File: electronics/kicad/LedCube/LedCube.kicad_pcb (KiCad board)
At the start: 2 copper layers, 20 parts, among them J1 Conn_01x03, J2 Conn_01x03, J3 Conn_01x03, J4 Conn_01x04, J5 COM, J6 Conn_01x02, J7 JTAG, U1 ESP32

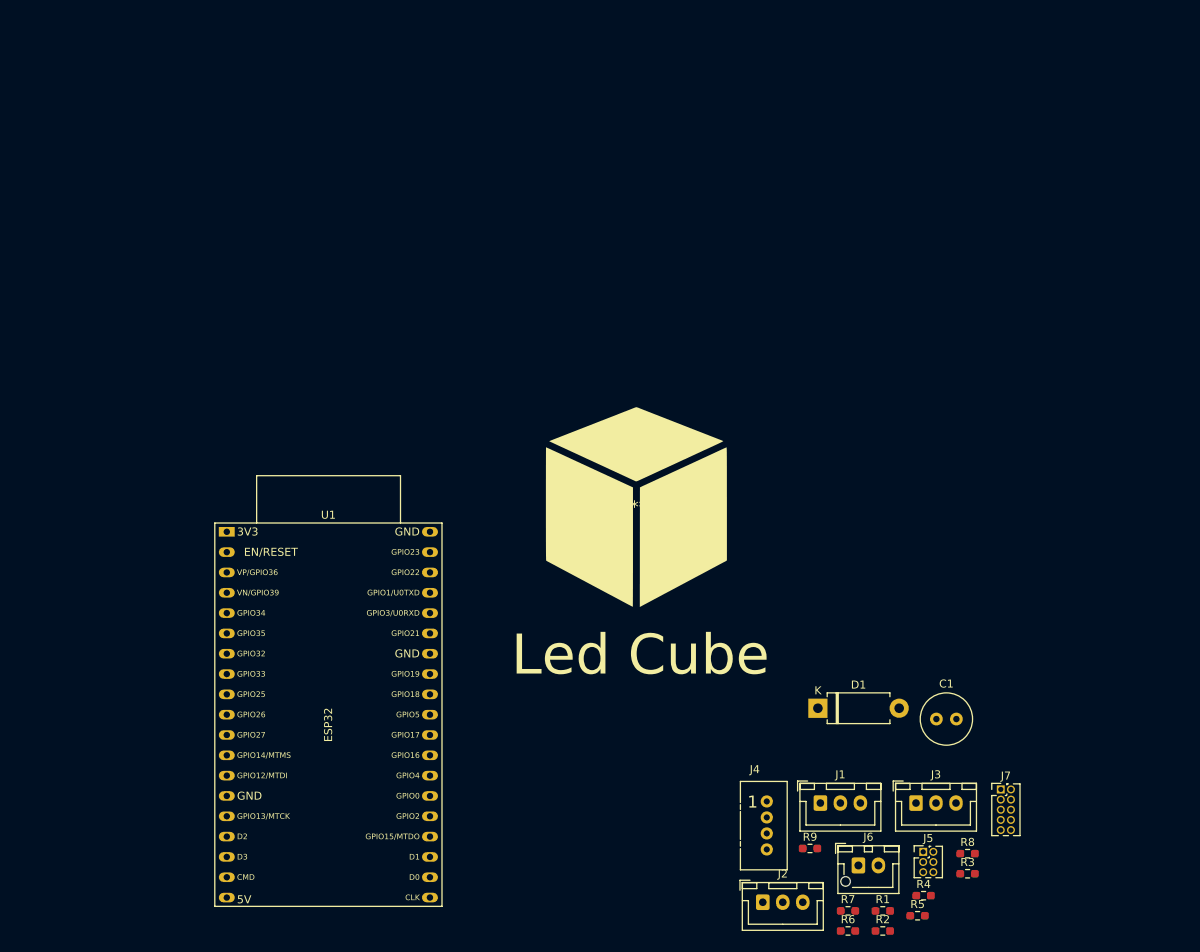
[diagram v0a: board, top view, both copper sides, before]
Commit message: Update to KiCad 7.0
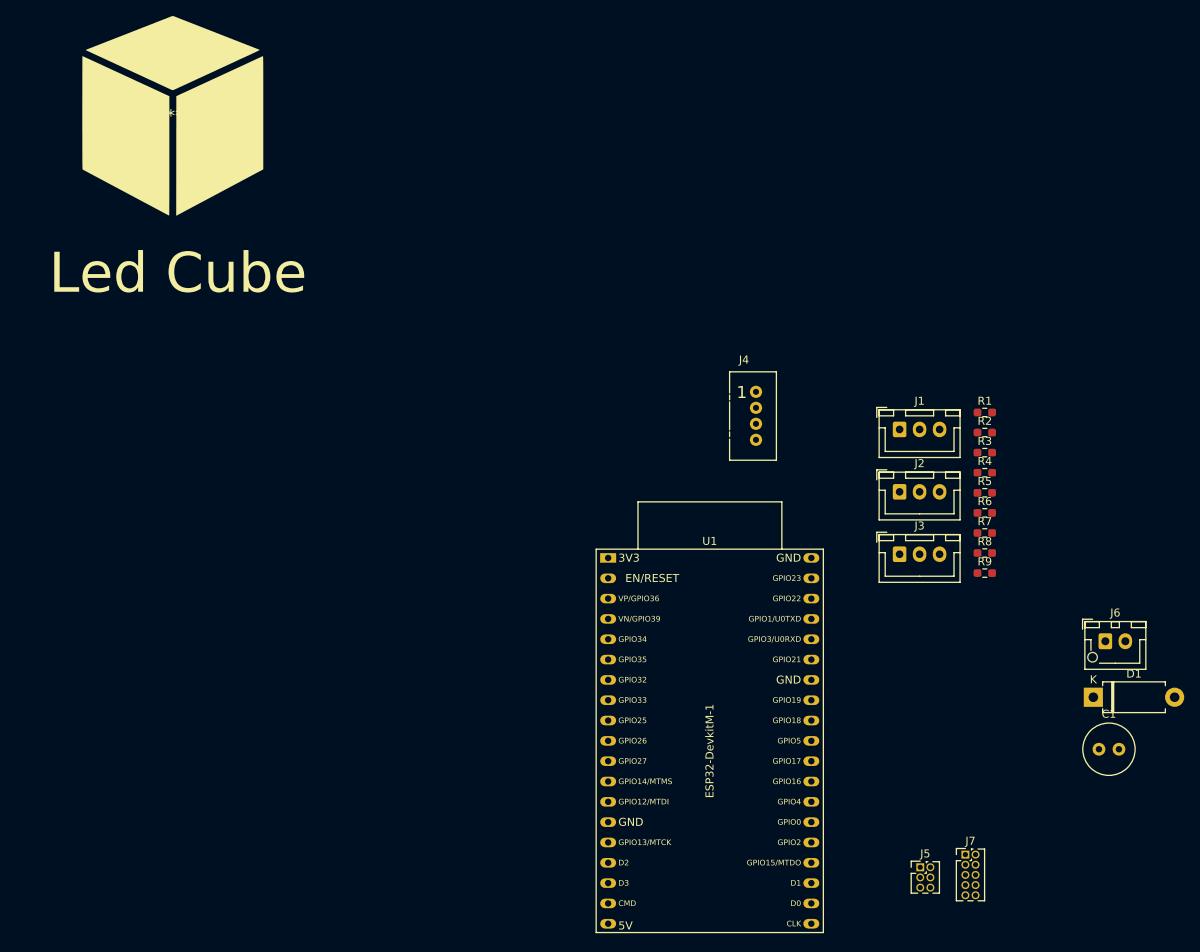
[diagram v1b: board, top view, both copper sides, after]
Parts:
- U1: value ESP32 -> ESP32-DevkitM-1
- moved G*** 75.8 mm to (54.0, 14.1)
- moved R1 63.6 mm to (155.6, 51.2)
- moved R2 63.6 mm to (155.6, 53.7)
- moved R6 55.0 mm to (155.6, 63.7)
- moved J2 54.1 mm to (144.9, 61.1)
- moved R5 53.5 mm to (155.6, 61.2)
- moved R4 53.4 mm to (155.6, 58.7)
- moved R3 52.7 mm to (155.6, 56.2)
- moved J4 51.2 mm to (127.0, 48.6)
- moved R7 50.2 mm to (155.6, 66.2)
- moved U1 47.8 mm to (108.5, 69.4)
- moved J1 47.7 mm to (144.9, 53.3)
- moved J6 41.7 mm to (170.6, 79.8)
- moved R9 40.8 mm to (155.6, 71.3)
- moved R8 37.6 mm to (155.6, 68.8)
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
